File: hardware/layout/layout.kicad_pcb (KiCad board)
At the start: 4 copper layers, 50 x 22 mm, 69 parts, among them J1 208658-1001, J2 USB4105-GF-A-060, SW1 TS-1088-AR02016, U1 PCA9306DCTR, U2 AP2112K-3.3TRG1, U3 USBLC6-2SC6, U4 W25Q16JVSSIQ, U5 RP2040, Y1 X322512MSB4SI

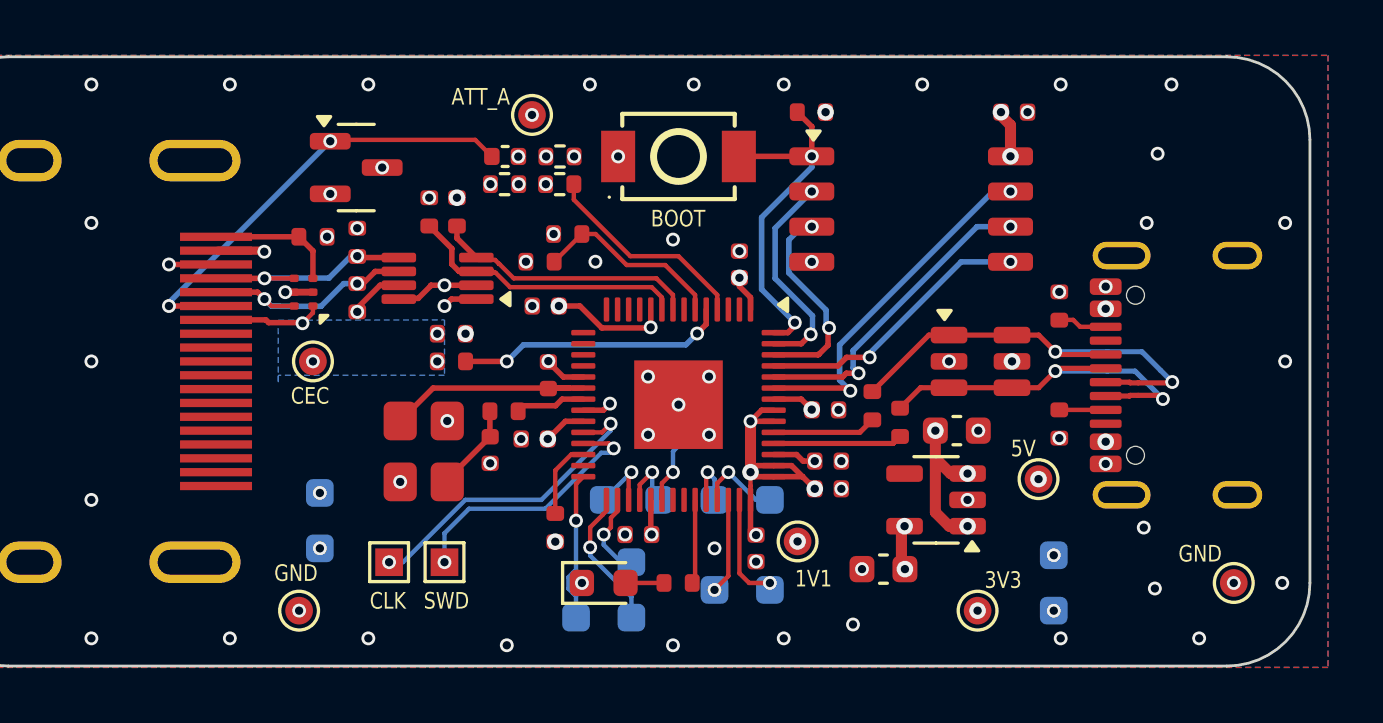
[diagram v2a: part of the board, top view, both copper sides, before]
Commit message: hardware: pre-production fixes (PCA9306 bias, HPD gate FET, BOOTSEL 1k, 33pF xtal caps)
Schematic review findings, all new parts JLC-Basic:
- PCA9306: EN+VREF2 shorted and biased from cable 5V via R12 200k + C2 100pF
  per TI SCPS113O (was: VREF2 hard-tied to 5V, EN to 3V3 - pass-FET damage
  risk and below the VREF1+0.6V enable minimum)
- HPD: Q1 2N7002 holds HPD low (gate pulled to 3V3 by R13 100k) until
  firmware drives new GP5/HPD_GATE low once the EDID slave is ready;
  unpowered board falls back to passive assert via R5
- BOOTSEL: R_BOOT 1k between QSPI_CS and SW1 per RP2040 design guide
- crystal: 15pF -> 33pF load caps to match YXC X322512MSB4SI CL=20pF
- cosmetics: D_ESD K3/K4 comment matches pins; Power module no longer
  shadows the Power() builtin

Layout re-synced (refdes renumbered, placement preserved), new parts
placed + routed; kicad-cli DRC: 0 violations, 0 unconnected.

NOTE firmware: GP5 must be driven low to release HPD or the board is
invisible to HDMI sources.
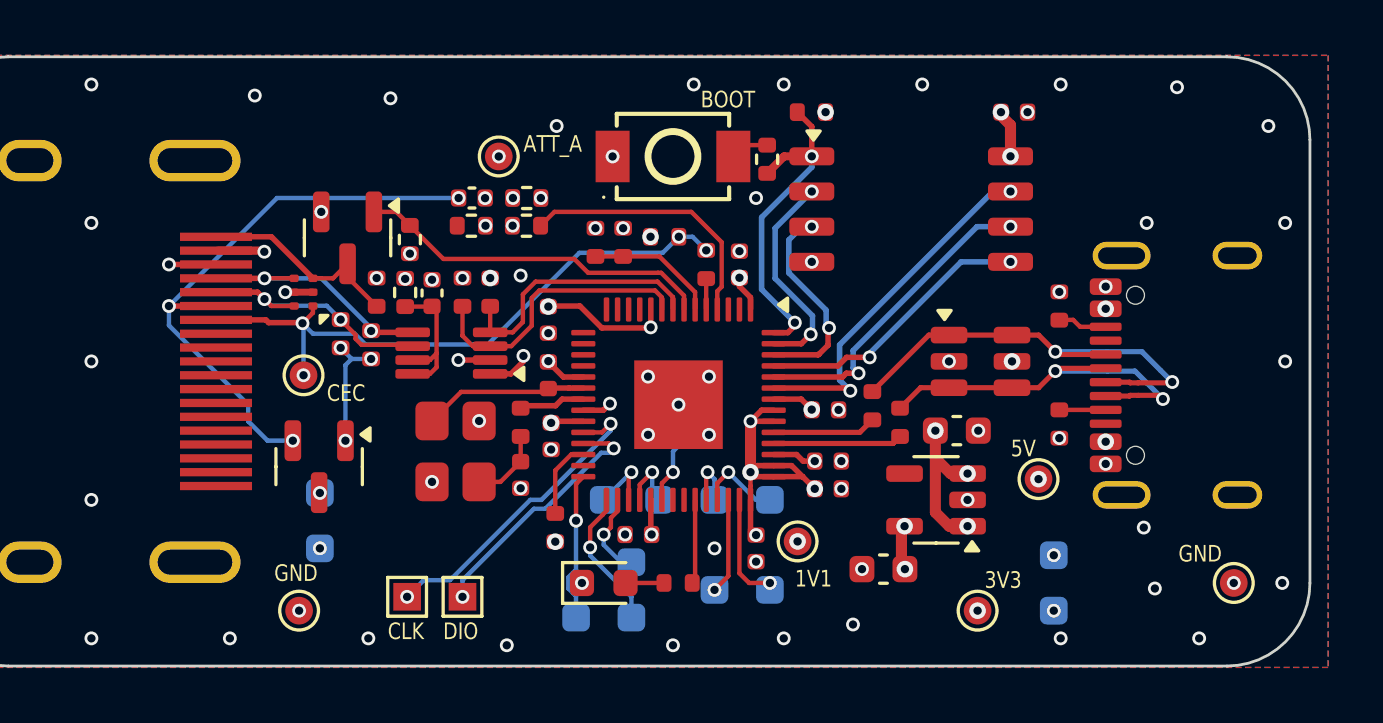
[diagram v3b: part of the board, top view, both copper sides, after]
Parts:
- added C2: 0402CG101J500NT, kicad_libraries_kicad-footprints_Capacitor_SMD@9.0.3:C_0402_1005Metric, F.Cu at (118.3, 108.5)
- added Q1: 2N7002, kicad_libraries_kicad-footprints_Package_TO_SOT_SMD@9.0.3:SOT-23, F.Cu at (115.2, 106.5)
- added R12: 0402WGF2003TCE, kicad_libraries_kicad-footprints_Resistor_SMD@9.0.3:R_0402_1005Metric, F.Cu at (117.3, 108.5)
- added R13: 0402WGF1003TCE, kicad_libraries_kicad-footprints_Resistor_SMD@9.0.3:R_0402_1005Metric, F.Cu at (117.5, 106.6)
- added R16: 0402WGF1001TCE, kicad_libraries_kicad-footprints_Resistor_SMD@9.0.3:R_0402_1005Metric, F.Cu at (130.4, 103.7)
- C14: renamed from C13; value 0402CG150J500NT -> 0402CG330J500NT
- C15: renamed from C14; value 0402CG150J500NT -> 0402CG330J500NT
- moved D3 10.9 mm to (114.2, 114.8), turned to -90 degrees
- moved R2 9.84 mm to (128.2, 107.5), turned to 90 degrees
- moved R1 8.46 mm to (126.7, 106.5), turned to 0 degrees
- moved R11 3.73 mm to (116.1, 110.4), turned to -90 degrees
- moved R8 3.14 mm to (119.4, 108.5)
- moved R9 3.14 mm to (120.4, 108.5)
- moved R5 3.05 mm to (116.3, 108.5), turned to -90 degrees
- moved U1 2.75 mm to (119.0, 110.7)
- moved R6 2.12 mm to (124.2, 106.7), turned to -90 degrees
- moved R7 2.02 mm to (125.2, 106.7), turned to 90 degrees
- moved C1 1.92 mm to (119.7, 105.1)
- moved R14 1.92 mm to (121.7, 105.1)
- moved R15 1.92 mm to (119.7, 106.1)
- moved R3 1.92 mm to (121.7, 106.1)
- moved TP18 1.92 mm to (120.7, 103.6)
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- renumbered C9 to C10, C10 to C11, C11 to C12, C12 to C13, C2 to C3, C3 to C4, C4 to C5, C5 to C6, C6 to C7, C7 to C8, C8 to C9, R12 to R14, R13 to R15, R14 to R17, R15 to R18, R16 to R19, R17 to R20, R18 to R21, R19 to R22, R20 to R23
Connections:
- D3 pad 1: HDMI._ARC14 -> HDMI._HDMI_5V
- D3 pad 2: HDMI._HDMI_5V -> HDMI._ARC14
- SW1 pad 1: QSPI_CS -> BOOTSEL_SW
- U1 pad 7: HDMI._HDMI_5V -> HDMI._VREF2_EN
- U1 pad 8: VDD_3V3 -> HDMI._VREF2_EN
- U5 pad 7: U_MCU.NC_GPIO5 -> HPD_GATE
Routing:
- net CEC_NODE: track 3.93 -> 22.5 mm
- net HPD_GATE: track 0.00 -> 13.0 mm
- net CEC_BUS: track 9.78 -> 1.11 mm, vias 2 -> 0
- net HDMI._VREF2_EN: track 0.00 -> 5.25 mm
- net HDMI._ARC14: track 16.2 -> 21.0 mm, vias 2 -> 3
- net HDMI._HPD: track 4.70 -> 7.56 mm
- net HDMI._HDMI_5V: track 3.85 -> 6.10 mm, vias 6 -> 7
- net HDMI_5V_SENSE: track 6.94 -> 4.76 mm
- net ARC_TX: track 7.69 -> 9.70 mm
- net U_MCU.oscpair_XIN: track 7.87 -> 5.96 mm
- net VDD_3V3: track 25.2 -> 23.8 mm, vias 21 -> 22
- net BOOTSEL_SW: track 0.00 -> 1.40 mm
- net DDC_SDA_5V: track 8.03 -> 9.05 mm
- net QSPI_CS: track 12.7 -> 11.9 mm
- net DDC_SCL_5V: track 8.63 -> 9.29 mm
- added copper zone on In2.Cu, net HDMI._HDMI_5V
- added copper zone on In2.Cu, net VDD_1V1
- added copper zone on In2.Cu, net VDD_5V
- removed copper zone on B.Cu, net CEC_NODE
- removed copper zone on In1.Cu, net HDMI._HDMI_5V
- removed copper zone on In1.Cu, net VDD_1V1
- removed copper zone on In1.Cu, net VDD_5V
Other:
- board text added: "DIO"
- board text removed: "SWD"

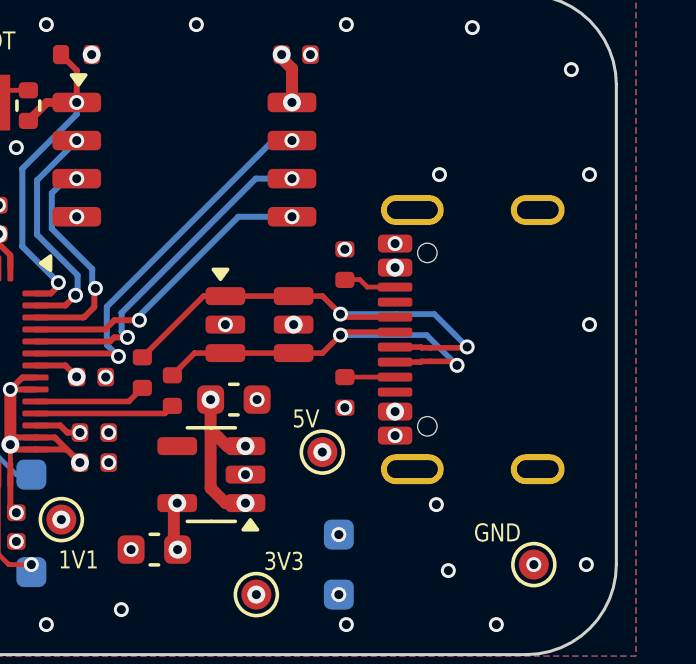
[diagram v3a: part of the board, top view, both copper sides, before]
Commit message: fix: center USB connector to the board
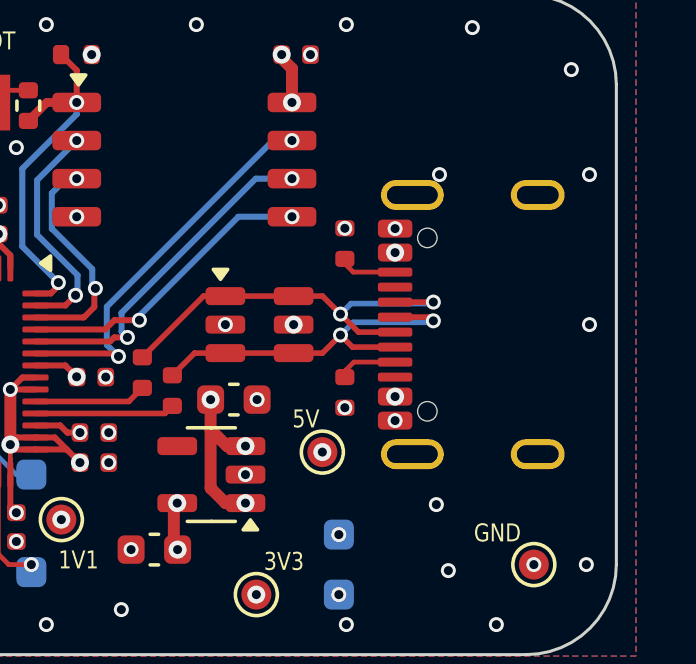
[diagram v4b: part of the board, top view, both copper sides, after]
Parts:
- moved R18 0.70 mm to (140.9, 108.3)
- moved J2 0.50 mm to (146.3, 111.0)
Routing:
- net USB_D_P: track 16.7 -> 14.3 mm
- net USB_D_N: track 14.5 -> 12.8 mm

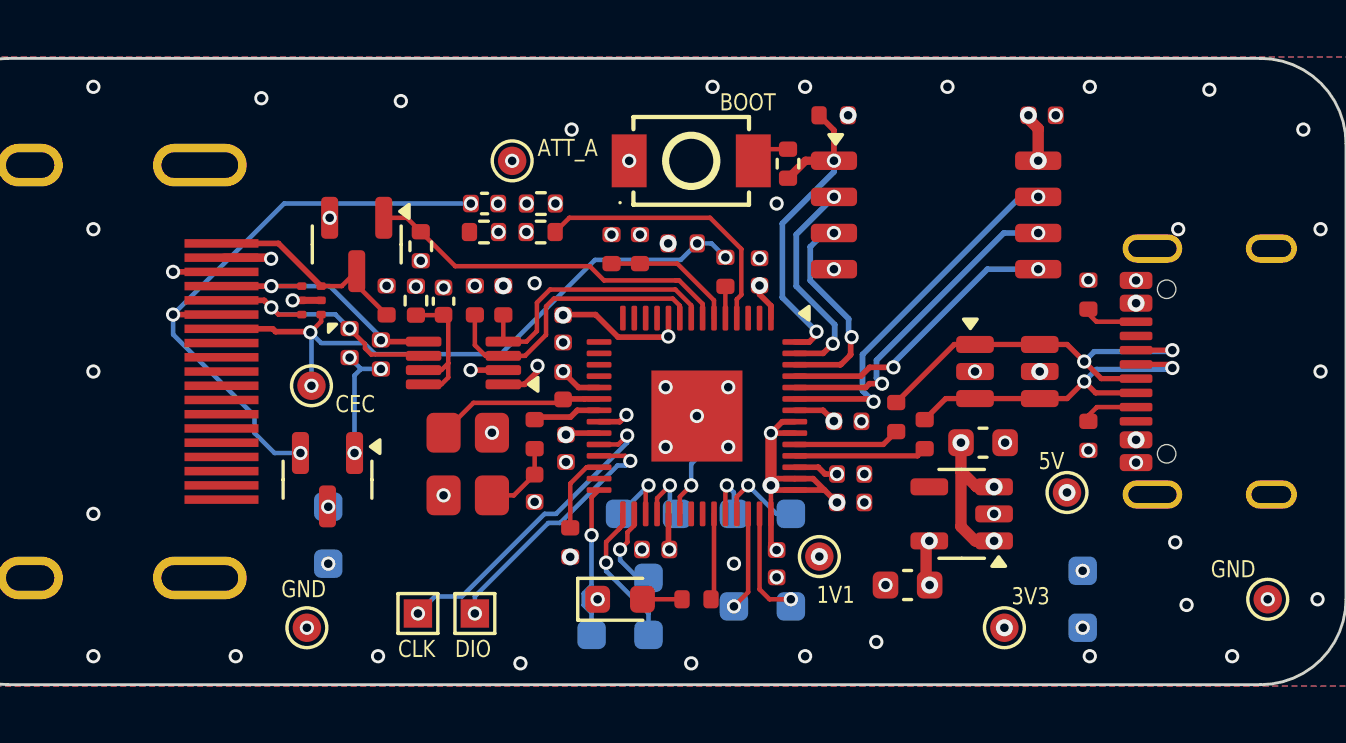
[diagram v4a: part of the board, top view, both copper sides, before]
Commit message: fix: reroute ATT_A in a less roundabout way
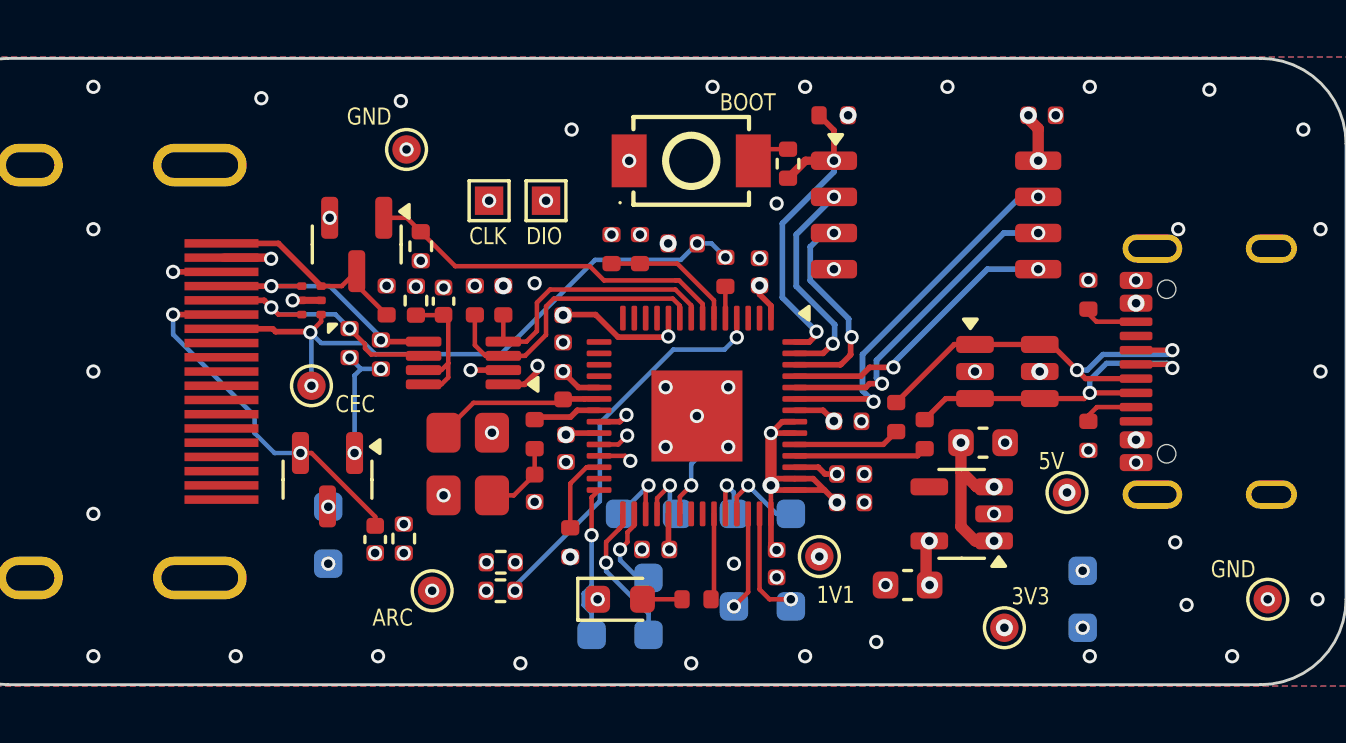
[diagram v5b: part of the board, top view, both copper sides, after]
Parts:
- moved TP21 17.2 mm to (117.0, 103.2)
- moved TP18 15.4 mm to (117.9, 118.7)
- moved TP22 14.7 mm to (119.9, 105.0)
- moved TP23 14.7 mm to (121.9, 105.0)
- moved R14 12.7 mm to (120.3, 117.7)
- moved R3 12.7 mm to (120.3, 118.7)
- moved C1 12.4 mm to (115.9, 116.9), turned to 90 degrees
- moved R15 11.1 mm to (116.9, 116.9), turned to 90 degrees
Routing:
- net HDMI._ARC14: track 21.0 -> 12.8 mm, vias 3 -> 2
- net ARC_TX: track 9.70 -> 13.9 mm, vias 0 -> 2
- net SWD_SWDIO: track 9.20 -> 12.1 mm
- net SWD_SWCLK: track 11.2 -> 12.5 mm
- net GND: vias 76 -> 77
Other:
- board text added: "ARC"
- board text removed: "ATT_A"

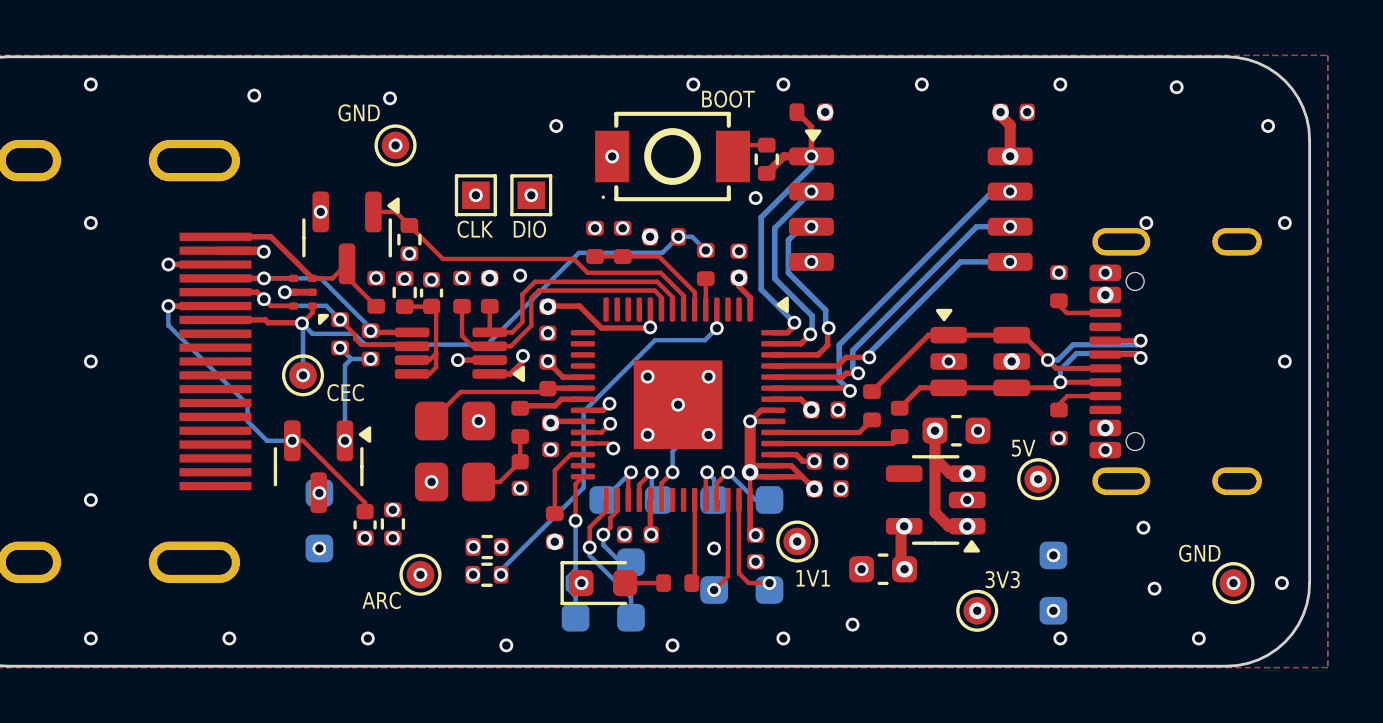
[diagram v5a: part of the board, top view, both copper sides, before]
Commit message: fix: no more vias in pads, @ivanlevsky should be proud
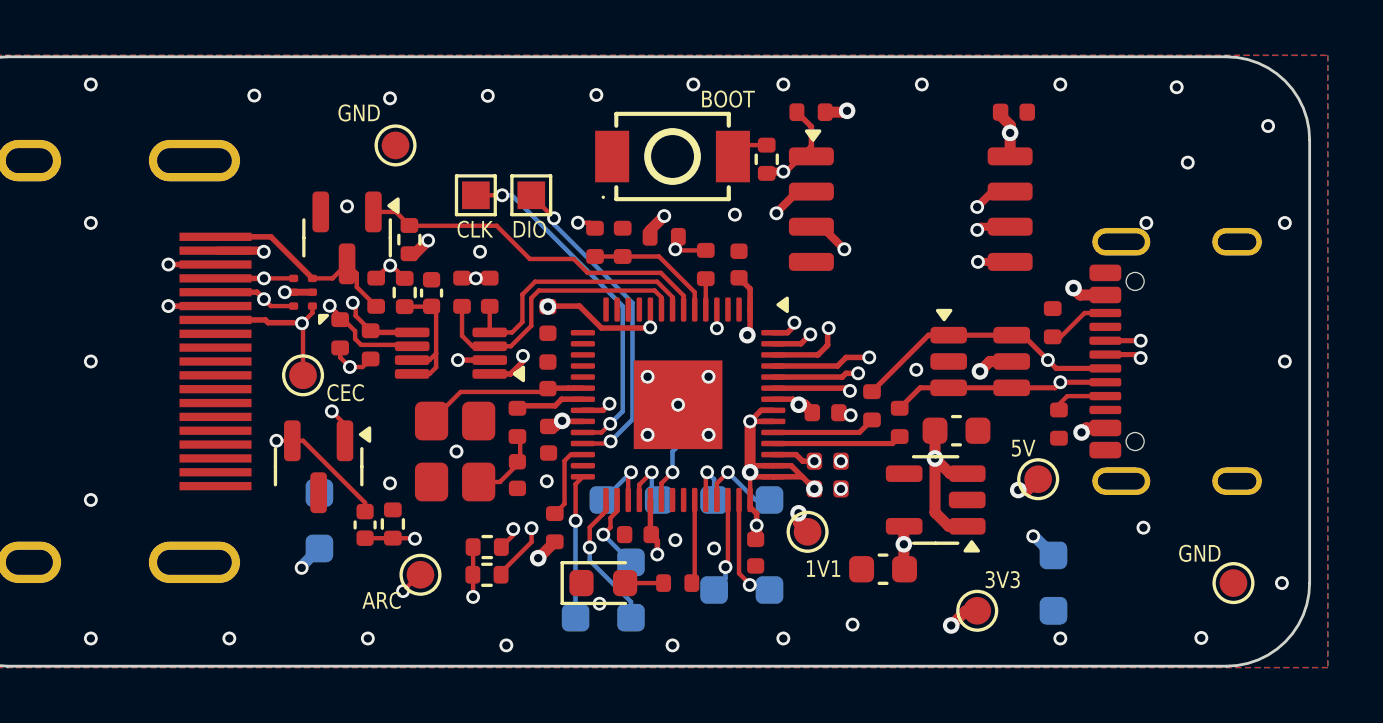
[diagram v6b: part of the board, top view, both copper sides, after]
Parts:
- moved R18 1.32 mm to (140.7, 109.6)
- moved TP15 0.51 mm to (131.9, 117.2)
- moved C13 0.15 mm to (130.0, 117.9)
- moved C6 0.15 mm to (122.5, 113.8)
- moved C8 0.10 mm to (132.5, 112.8)
- moved C15 0.10 mm to (121.4, 115.1)
- moved R23 0.10 mm to (121.4, 113.2)
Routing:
- net VDD_3V3: track 23.8 -> 31.9 mm, vias 22 -> 19
- net VDD_5V: track 5.75 -> 11.1 mm, vias 8 -> 6
- net ATT_A: track 0.00 -> 4.48 mm, vias 5 -> 3
- net QSPI_CS: track 11.9 -> 10.7 mm
- net VDD_1V1: track 4.31 -> 5.32 mm
- net HDMI._HDMI_5V: track 6.10 -> 6.81 mm, vias 7 -> 5
- net GND: track 5.45 -> 4.79 mm, vias 77 -> 56
- net ARC_TX: track 13.9 -> 13.2 mm
- net CEC_NODE: track 22.5 -> 22.9 mm, vias 4 -> 2

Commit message: fix: I like to move it move it
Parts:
- moved TP20 2.30 mm to (144.9, 119.0)
- moved TP21 0.91 mm to (117.8, 103.7)
- moved R19 0.51 mm to (132.5, 102.0)
- moved C5 0.36 mm to (139.7, 102.0)
- moved C15 0.10 mm to (121.5, 115.1)
- moved R23 0.10 mm to (121.5, 113.2)
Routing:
- net GND: track 4.79 -> 2.38 mm, vias 56 -> 39
- net ATT_A: track 4.48 -> 2.88 mm
- net CEC_NODE: track 22.9 -> 23.7 mm
